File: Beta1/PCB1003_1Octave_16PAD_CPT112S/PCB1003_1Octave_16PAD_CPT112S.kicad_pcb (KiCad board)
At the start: 2 copper layers, 188.9 x 64 mm, 101 parts, among them U1 CPT112S, U100 CPT112S, U200 CPT112S

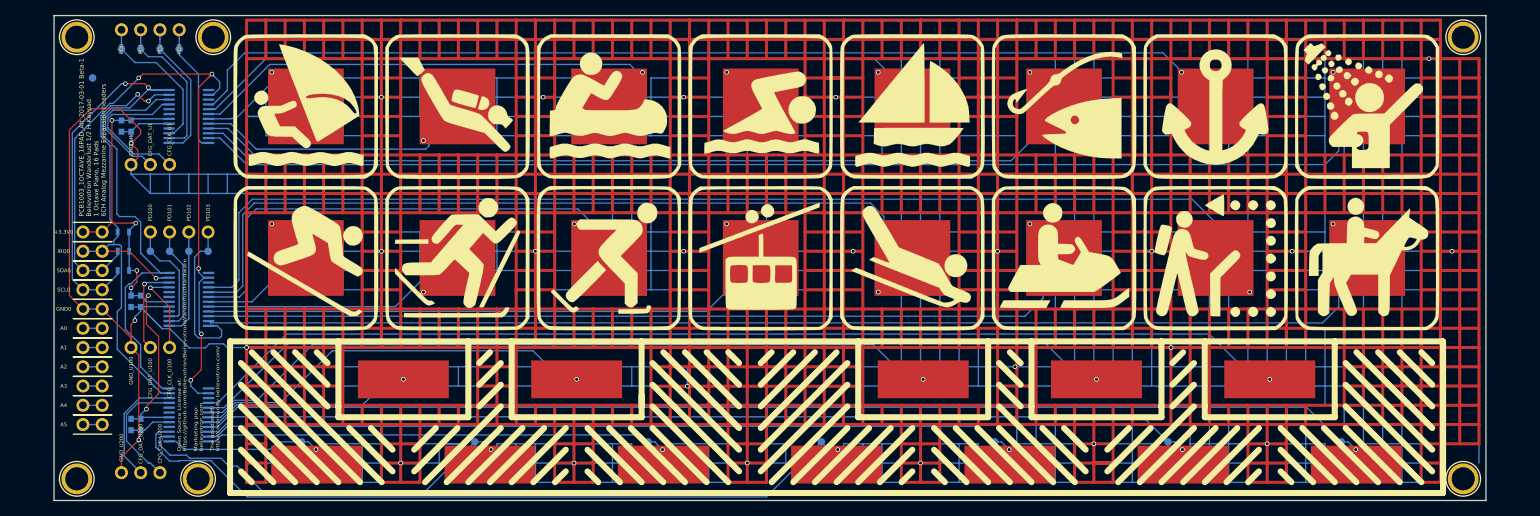
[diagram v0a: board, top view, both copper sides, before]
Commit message: Renamed. Widened from 36U to 38U. Ready for Fab.
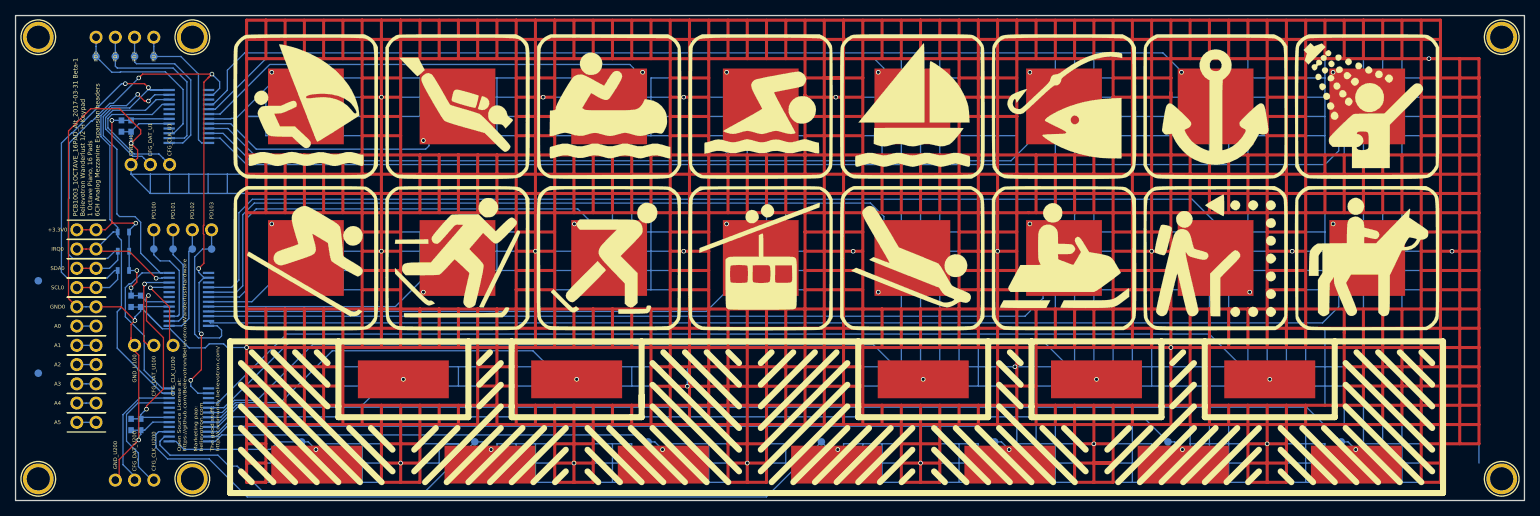
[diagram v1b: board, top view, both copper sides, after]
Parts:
- added REF**: Fiducial_1mm_Dia_2.54mm_Outer_CopperBottom, Fiducials:Fiducial_1mm_Dia_2.54mm_Outer_CopperBottom, F.Cu at (7.62, -43.7)
- moved REF** 5.08 mm to (193.5, -3.00)
- moved REF** 5.08 mm to (193.5, -61.2)
- moved REF** 5.08 mm to (0.46, -61.2)
- moved REF** 5.08 mm to (0.46, -3.00)
- moved PD1 3.49 mm to (10.6, -61.2)
- moved PD2 3.49 mm to (13.2, -61.2)
- moved PD3 3.49 mm to (15.7, -61.2)
- moved TP1 3.49 mm to (10.6, -58.7)
- moved TP2 3.49 mm to (13.2, -58.7)
- moved TP3 3.49 mm to (15.7, -58.7)
- moved PD0 3.49 mm to (8.08, -61.2)
- moved TP0 3.49 mm to (8.08, -58.7)
- moved REF** 2.76 mm to (20.8, -61.2)
- moved CFG_CLK_U200 1.27 mm to (15.7, -2.83)
- moved CFG_DAT_U200 1.27 mm to (13.2, -2.83)
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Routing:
- net /SCL: track 101.1 -> 108.1 mm
- net /SDA: track 96.3 -> 102.4 mm
- net Net-(PD1-Pad1): track 20.7 -> 24.4 mm
- net Net-(PD2-Pad1): track 18.9 -> 22.2 mm
- net Net-(PD0-Pad1): track 19.8 -> 22.8 mm
- net Net-(PD3-Pad1): track 17.1 -> 19.6 mm
- net +3V3: track 69.4 -> 70.7 mm
- net GND: track 9573.3 -> 9574.6 mm
- net Net-(PD103-Pad1): track 21.4 -> 22.6 mm
- net Net-(PD102-Pad1): track 15.0 -> 16.3 mm
- net /IRQ: track 67.9 -> 68.9 mm
- net Net-(CFG_DAT_U200-Pad1): track 15.5 -> 16.3 mm
- net Net-(PD101-Pad1): track 14.0 -> 14.7 mm
- net Net-(PD100-Pad1): track 14.7 -> 15.4 mm
- net Net-(CFG_CLK_U200-Pad1): track 15.9 -> 16.6 mm
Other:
- board size 188.9 x 64 mm -> 199 x 64 mm
- board text added: "Open source MIT license files at: github.com/Believotron/BelievotronWanderlustHardware Replacement parts, upgrades, updates, new gear, and marketing pap: Believotron.com For help, bug reporting, dev-blogs, or joy at your bonkers-cool creation, the good stuff is here: community.believotron.com"
- board text added: "PCB1003_1OCTAVE_16PAD_Alt_2017-03-31 Beta-1 Believotron Wanderlust 1/2 H Keypad 1 Octave Piano, 16 Pads 6CH Analog Mezzanine Expansion headers"
- board text removed: "PCB1003_1OCTAVE_16PAD_Alt_2017-03-01 Beta-1 Believotron Wanderlust 1/2 H Keypad 1 Octave Piano, 16 Pads 6CH Analog Mezzanine Expansion headers"
